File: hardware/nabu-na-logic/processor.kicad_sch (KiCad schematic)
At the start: 16 parts, among them U17 2114, U18 2114, U31 MC6805P2, U5 8x60, U6 74LS374, U7 74LS373, U8 ?, U9 TR1863

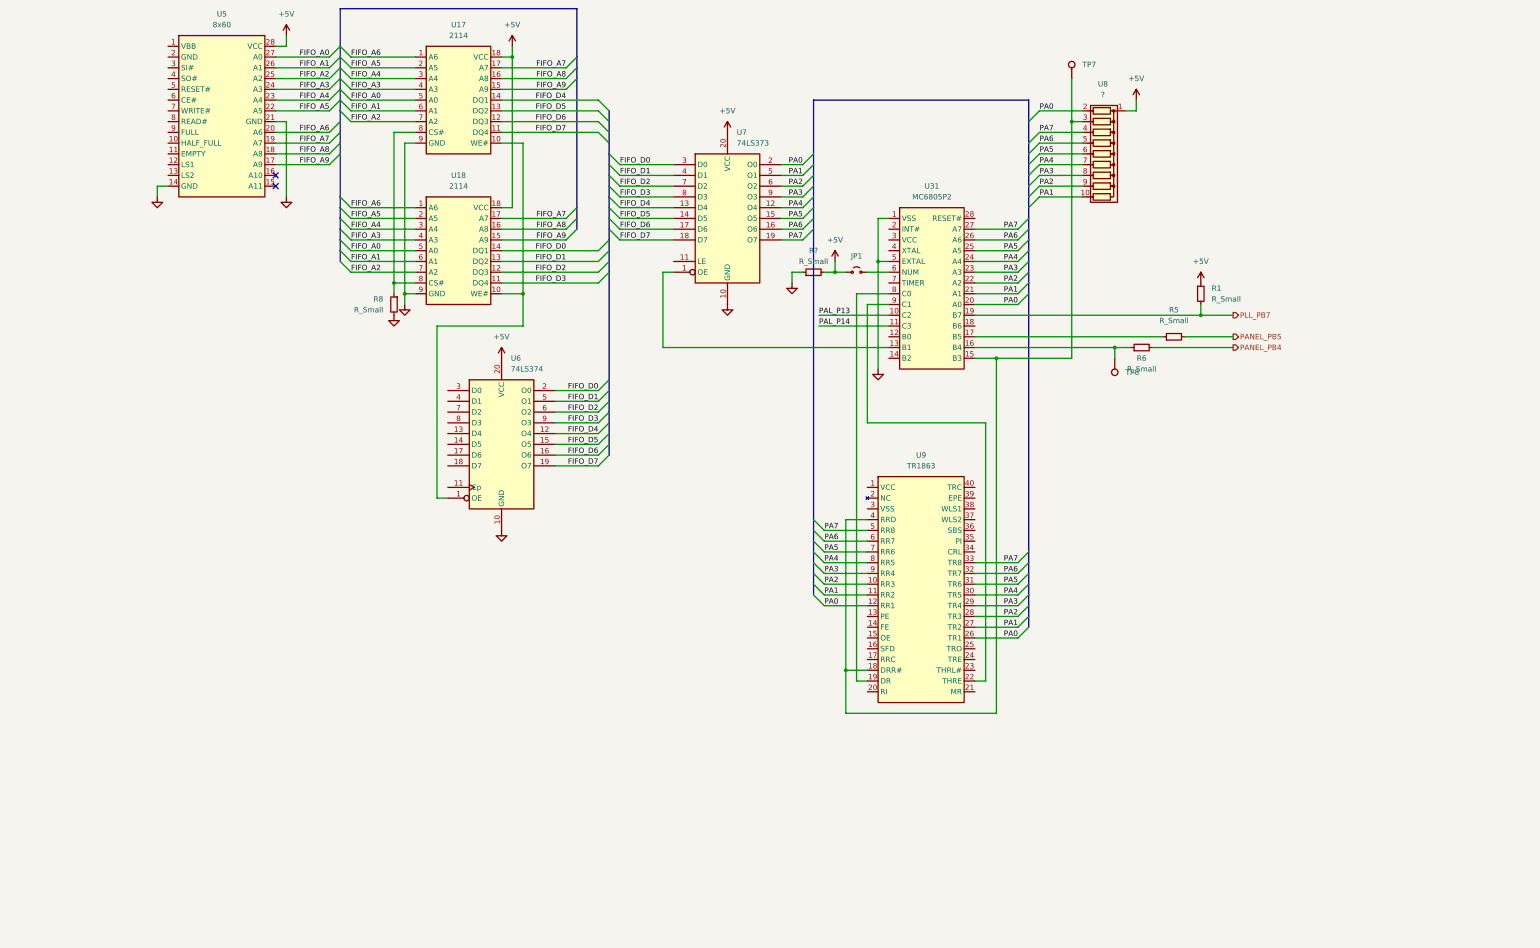
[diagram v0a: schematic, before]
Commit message: Logic board schematic: Add PAL, assorted changes I've forgotten already.
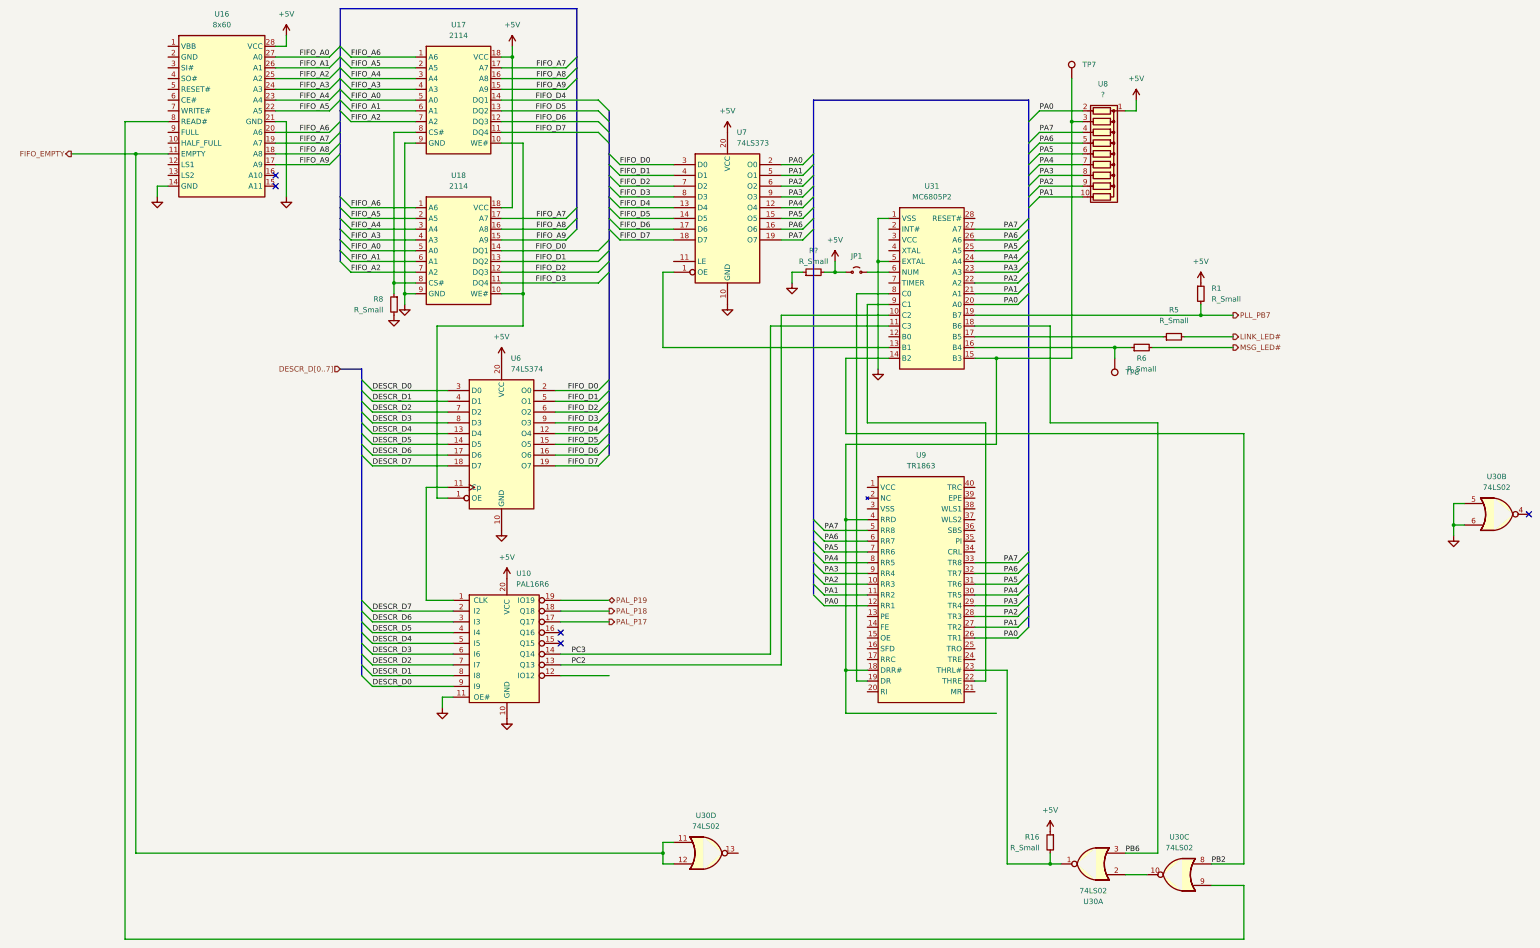
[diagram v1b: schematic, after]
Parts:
- added R16: R_Small, symbol Device:R_Small
- added U10: PAL16R6, symbol mmi:PAL16R6
- added U30: 74LS02, symbol 74xx:74LS02
- renumbered U5 to U16
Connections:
- net +5V: now also R16.1, U10.20 (VCC)
- net GND: now also U10.10 (GND), U10.11 (OE#), U30.5, U30.6
- net PB2: now reaches U31.14 (B2)
- net PB2: now also U30.8
- net PB6: now reaches U31.18 (B6)
- net PB6: now also U30.3
- net at U9.23 (THRL#): now also R16.2, U30.1
- net at U6.11 (Cp): now also U10.1 (CLK)
- net DESCR_D4: now reaches U6.13 (D4)
- net DESCR_D4: now also U10.5 (I5)
- net DESCR_D5: now reaches U6.14 (D5)
- net DESCR_D5: now also U10.4 (I4)
- net DESCR_D6: now reaches U6.17 (D6)
- net DESCR_D6: now also U10.3 (I3)
- net DESCR_D7: now reaches U6.18 (D7)
- net DESCR_D7: now also U10.2 (I2)
- net DESCR_D0: now reaches U6.3 (D0)
- net DESCR_D0: now also U10.9 (I9)
- net DESCR_D1: now reaches U6.4 (D1)
- net DESCR_D1: now also U10.8 (I8)
- net DESCR_D2: now reaches U6.7 (D2)
- net DESCR_D2: now also U10.7 (I7)
- net DESCR_D3: now reaches U6.8 (D3)
- net DESCR_D3: now also U10.6 (I6)
- net FIFO_EMPTY: now reaches U16.11 (EMPTY)
- net FIFO_EMPTY: now also U30.11, U30.12
- net at U16.8 (READ#): now also U30.9
- net PAL_P13 renamed PC2
- net PC2: now also U10.13 (Q13)
- net PAL_P14 renamed PC3
- net PC3: now also U10.14 (Q14)
- net PANEL_PB4 renamed MSG_LED#
- net PANEL_PB5 renamed LINK_LED#
- new net: U30.10, U30.2
- new net PAL_P17: U10.17 (Q17)
- new net PAL_P18: U10.18 (Q18)
- new net PAL_P19: U10.19 (IO19)
- no-connect marks 2 -> 5
